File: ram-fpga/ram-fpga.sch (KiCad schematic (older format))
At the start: 9 parts, among them J1 Conn_02x20_Odd_Even, U1 27128, U2 27128, U3 MC74LVXC3245, U4 MC74LVXC3245, U5 MC74LVXC3245, U6 MC74LVXC3245

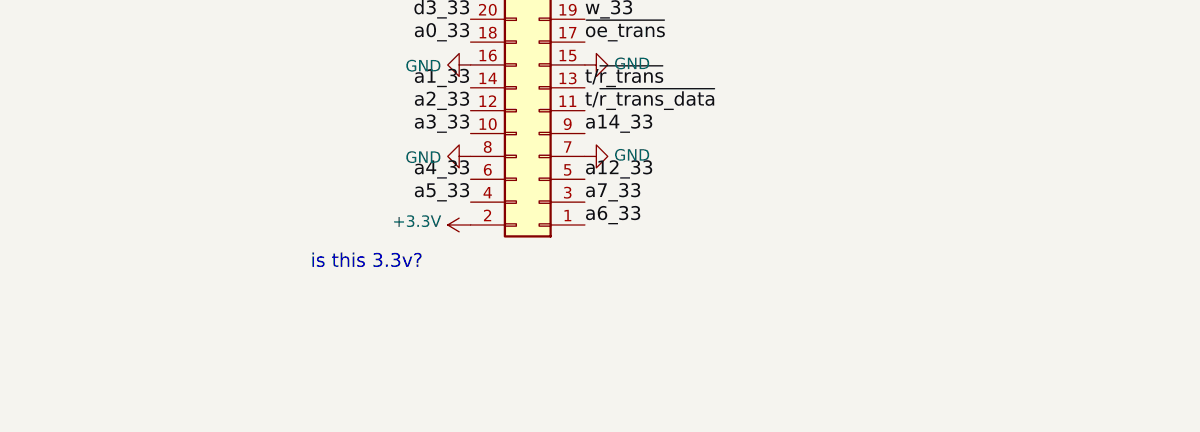
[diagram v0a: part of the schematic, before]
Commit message: switch to smt header
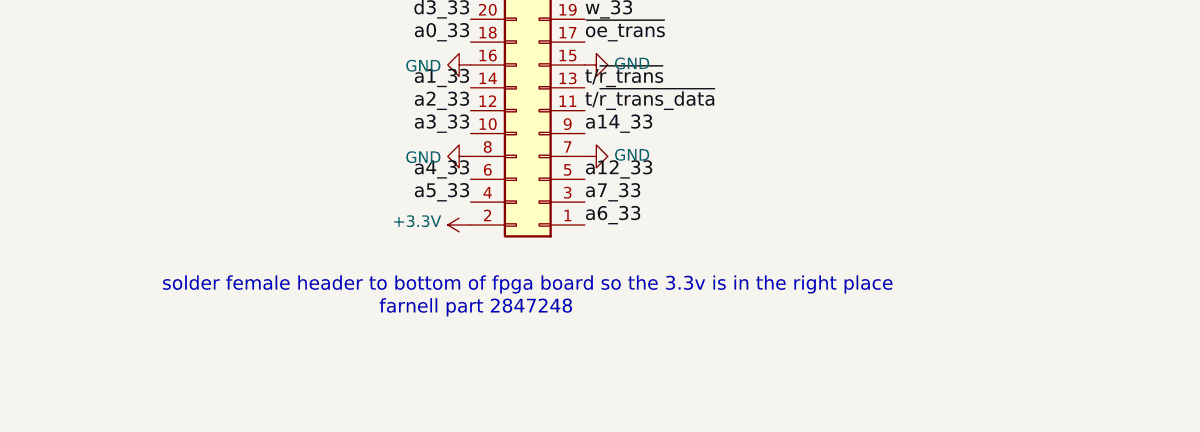
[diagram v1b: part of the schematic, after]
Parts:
- J1: footprint Connector_IDC:IDC-Header_2x20_P2.54mm_Vertical -> Connector_PinHeader_2.54mm:PinHeader_2x20_P2.54mm_Vertical_SMD; MOQ (none) -> Value; leadtime (none) -> Value; supplier (none) -> Value; supplier PN (none) -> Value
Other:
- note added: "farnell part 2847248"
- note added: "solder female header to bottom of fpga board so the 3.3v is in the right place"
- note removed: "is this 3.3v?"
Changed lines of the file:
@@
 F 0 "J1" H 8100 3475 50  0000 C CNN
 F 1 "Conn_02x20_Odd_Even" H 8100 3566 50  0000 C CNN
-F 2 "Connector_IDC:IDC-Header_2x20_P2.54mm_Vertical" H 8050 4700 50  0001 C CNN
+F 2 "Connector_PinHeader_2.54mm:PinHeader_2x20_P2.54mm_Vertical_SMD" H 8050 4700 50  0001 C CNN
 F 3 "~" H 8050 4700 50  0001 C CNN
+F 4 "Value" H 8050 4700 60  0001 C CNN "supplier"
+F 5 "Value" H 8050 4700 60  0001 C CNN "supplier PN"
+F 6 "Value" H 8050 4700 60  0001 C CNN "MOQ"
+F 7 "Value" H 8050 4700 60  0001 C CNN "leadtime"
 	1    8050 4700
 	-1   0    0    1
@@
 	-1   0    0    1
 $EndComp
-Text Notes 7050 5800 0    60   ~ 0
-is this 3.3v?
 $Comp
 L Test_Point TP2
@@
 Text Label 8250 5100 0    60   ~ 0
 t/~r_trans_data
+Text Notes 6400 5900 0    60   ~ 0
+solder female header to bottom of fpga board so the 3.3v is in the right place
+Text Notes 7350 6000 0    60   ~ 0
+farnell part 2847248
 $EndSCHEMATC
